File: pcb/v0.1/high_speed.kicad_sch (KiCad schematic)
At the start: 16 parts, among them J4 TYPE_C_Receptacle, J5 TYPE_C_Receptacle, J7 Conn_01x22_Female, U8 AP22653W6-7

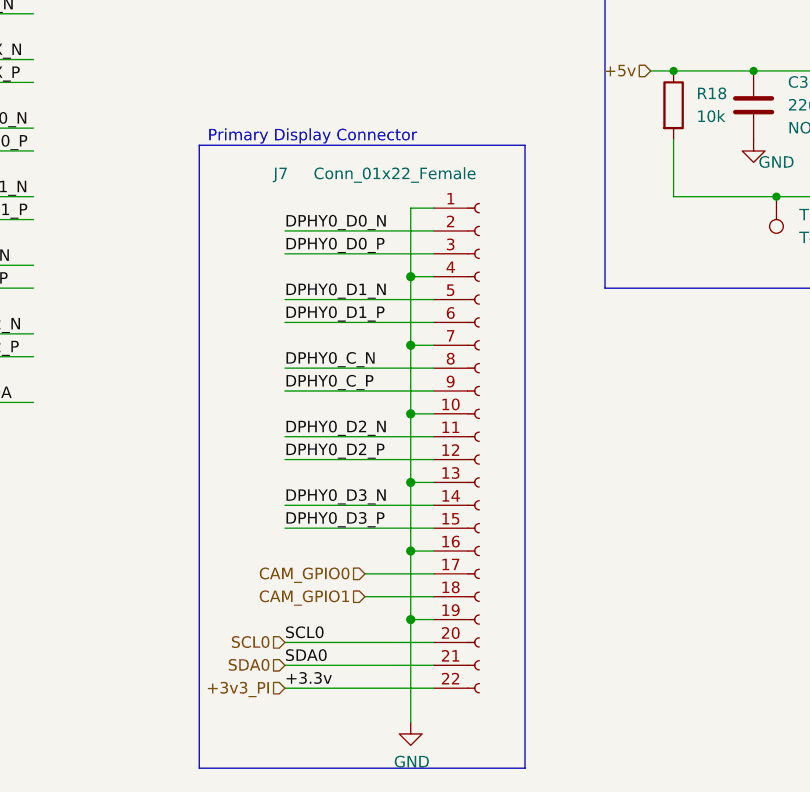
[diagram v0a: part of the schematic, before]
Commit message: Add display connector
The zephyr version is irrelevant now
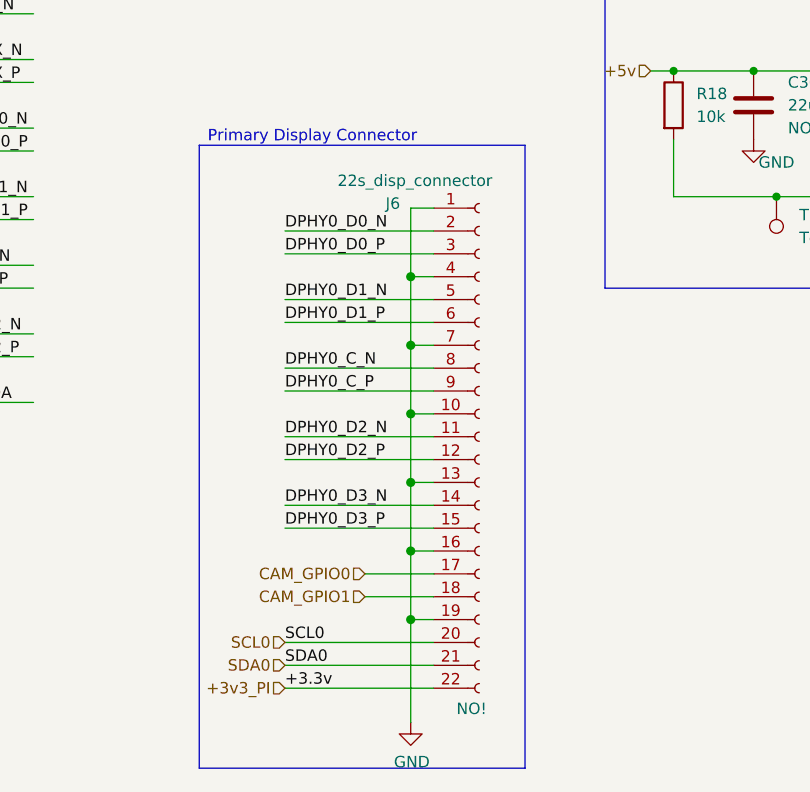
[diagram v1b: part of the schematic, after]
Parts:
- removed J7: Conn_01x22_Female, CM5IO:Hirose_FH12-22S-0.5SH_1x22-1MP_P0.50mm_Horizontal, symbol Connector:Conn_01x22_Socket
- added J6: 22s_disp_connector, symbol TH-1-CC:22s_disp_connector
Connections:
- net +3v3_PI: now also J6.22 (Pin_22)
- net CAM_GPIO0: now also J6.17 (Pin_17)
- net CAM_GPIO1: now also J6.18 (Pin_18)
- net DPHY0_C_N: now also J6.8 (Pin_8)
- net DPHY0_C_P: now also J6.9 (Pin_9)
- net DPHY0_D0_N: now also J6.2 (Pin_2)
- net DPHY0_D0_P: now also J6.3 (Pin_3)
- net DPHY0_D1_N: now also J6.5 (Pin_5)
- net DPHY0_D1_P: now also J6.6 (Pin_6)
- net DPHY0_D2_N: now also J6.11 (Pin_11)
- net DPHY0_D2_P: now also J6.12 (Pin_12)
- net DPHY0_D3_N: now also J6.14 (Pin_14)
- net DPHY0_D3_P: now also J6.15 (Pin_15)
- net GND: now also J6.1 (Pin_1), J6.10 (Pin_10), J6.13 (Pin_13), J6.16 (Pin_16), J6.19 (Pin_19), J6.4 (Pin_4), J6.7 (Pin_7)
- net SCL0: now also J6.20 (Pin_20)
- net SDA0: now also J6.21 (Pin_21)
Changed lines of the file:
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@@
-	)
-	(symbol
-		(lib_id "Connector:Conn_01x22_Socket")
-		(at 167.64 156.21 0)
-		(unit 1)
-		(body_style 1)
-		(exclude_from_sim no)
-		(in_bom yes)
-		(on_board yes)
-		(in_pos_files yes)
-		(dnp no)
-		(property "Reference" "J7"
-			(at 144.78 127 0)
-			(show_name no)
-			(do_not_autoplace no)
-			(effects
-				(font
-					(size 1.27 1.27)
-				)
-				(justify left)
-			)
-		)
-		(property "Value" "Conn_01x22_Female"
-			(at 149.225 127 0)
-			(show_name no)
-			(do_not_autoplace no)
-			(effects
-				(font
-					(size 1.27 1.27)
-				)
-				(justify left)
-			)
-		)
-		(property "Footprint" "CM5IO:Hirose_FH12-22S-0.5SH_1x22-1MP_P0.50mm_Horizontal"
-			(at 167.64 156.21 0)
-			(hide yes)
-			(show_name no)
-			(do_not_autoplace no)
-			(effects
-				(font
-					(size 1.27 1.27)
-				)
-			)
-		)
-		(property "Datasheet" "https://www.hirose.com/product/document?clcode=&productname=&series=FH12&documenttype=Catalog&lang=en&documentid=D31648_en"
-			(at 167.64 156.21 0)
-			(hide yes)
-			(show_name no)
-			(do_not_autoplace no)
-			(effects
-				(font
-					(size 1.27 1.27)
-				)
-			)
-		)
-		(property "Description" ""
-			(at 167.64 156.21 0)
-			(hide yes)
-			(show_name no)
-			(do_not_autoplace no)
-			(effects
-				(font
-					(size 1.27 1.27)
-				)
-			)
-		)
-		(property "Field4" "Mouser"
-			(at 167.64 156.21 0)
-			(hide yes)
-			(show_name no)
-			(do_not_autoplace no)
-			(effects
-				(font
-					(size 1.27 1.27)
-				)
-			)
-		)
-		(property "Field5" "798-FH12-22S-0.5SH55"
-			(at 167.64 156.21 0)
-			(hide yes)
-			(show_name no)
-			(do_not_autoplace no)
-			(effects
-				(font
-					(size 1.27 1.27)
-				)
-			)
-		)
-		(property "Field6" "FH12-22S-0.5SH55"
-			(at 167.64 156.21 0)
-			(hide yes)
-			(show_name no)
-			(do_not_autoplace no)
-			(effects
-				(font
-					(size 1.27 1.27)
-				)
-			)
-		)
-		(property "Field7" "Hirose"
-			(at 167.64 156.21 0)
-			(hide yes)
-			(show_name no)
-			(do_not_autoplace no)
-			(effects
-				(font
-					(size 1.27 1.27)
-				)
-			)
-		)
-		(property "Part Description" "22 Position FFC, FPC Connector Contacts, Bottom 0.020\" (0.50mm) Surface Mount, Right Angle"
-			(at 167.64 156.21 0)
-			(hide yes)
-			(show_name no)
-			(do_not_autoplace no)
-			(effects
-				(font
-					(size 1.27 1.27)
-				)
-			)
-		)
-		(pin "1"
-		)
-		(pin "10"
-		)
-		(pin "11"
-		)
-		(pin "12"
-		)
-		(pin "13"
-		)
-		(pin "14"
-		)
-		(pin "15"
-		)
-		(pin "16"
-		)
-		(pin "17"
-		)
-		(pin "18"
-		)
-		(pin "19"
-		)
-		(pin "2"
-		)
-		(pin "20"
-		)
-		(pin "21"
-		)
-		(pin "22"
-		)
-		(pin "3"
-		)
-		(pin "4"
-		)
-		(pin "5"
-		)
-		(pin "6"
-		)
-		(pin "7"
-		)
-		(pin "8"
-		)
-		(pin "9"
-		)
-		(instances
-			(project "mainboard"
-				(path "/5b8aa782-5c3d-43e7-a869-3bd000015f52/8e613e76-cfa9-4d70-9fba-6dbea9bbdbc9"
-					(reference "J7")
-					(unit 1)
-				)
-			)
-		)
 	)
 	(symbol
@@
 					(unit 1)
 				)
+			)
+		)
+	)
+	(symbol
+		(lib_id "TH-1-CC:22s_disp_connector")
+		(at 167.64 156.21 0)
+		(unit 1)
+		(body_style 1)
+		(exclude_from_sim no)
+		(in_bom yes)
+		(on_board yes)
+		(in_pos_files yes)
+		(dnp no)
+		(property "Reference" "J6"
+			(at 157.226 130.302 0)
+			(show_name no)
+			(do_not_autoplace no)
+			(effects
+				(font
+					(size 1.27 1.27)
+				)
+				(justify left)
+			)
+		)
+		(property "Value" "22s_disp_connector"
+			(at 151.892 127.762 0)
+			(show_name no)
+			(do_not_autoplace no)
+			(effects
+				(font
+					(size 1.27 1.27)
+				)
+				(justify left)
+			)
+		)
+		(property "Footprint" ""
+			(at 167.64 156.21 0)
+			(hide yes)
+			(show_name no)
+			(do_not_autoplace no)
+			(effects
+				(font
+					(size 1.27 1.27)
+				)
+			)
+		)
+		(property "Datasheet" "https://cdn.amphenol-cs.com/media/wysiwyg/files/documentation/datasheet/flex/flexconnectors_050mm_vll.pdf"
+			(at 167.64 156.21 0)
+			(hide yes)
+			(show_name no)
+			(do_not_autoplace no)
+			(effects
+				(font
+					(size 1.27 1.27)
+				)
+			)
+		)
+		(property "Description" "CONN FPC BOTTOM 22POS 0.5MM R/A"
+			(at 167.64 156.21 0)
+			(hide yes)
+			(show_name no)
+			(do_not_autoplace no)
+			(effects
+				(font
+					(size 1.27 1.27)
+				)
+			)
+		)
+		(property "Manufacturer" "Amphenol ICC (FCI)"
+			(at 167.64 156.21 0)
+			(hide yes)
+			(show_name no)
+			(do_not_autoplace no)
+			(effects
+				(font
+					(size 1.27 1.27)
+				)
+			)
+		)
+		(property "Mfr. Part no." "10051922-2210ELF"
+			(at 167.64 156.21 0)
+			(hide yes)
+			(show_name no)
+			(do_not_autoplace no)
+			(effects
+				(font
+					(size 1.27 1.27)
+				)
+			)
+		)
+		(property "Distributor DigiKey" "https://www.digikey.co.uk/en/products/detail/amphenol-cs-fci/10051922-2210ELF/4238683"
+			(at 167.64 156.21 0)
+			(hide yes)
+			(show_name no)
+			(do_not_autoplace no)
+			(effects
+				(font
+					(size 1.27 1.27)
+				)
+			)
+		)
+		(property "Digikey Part no." "609-10051922-2210ELFTR-ND"
+			(at 167.64 156.21 0)
+			(hide yes)
+			(show_name no)
+			(do_not_autoplace no)
+			(effects
+				(font
+					(size 1.27 1.27)
+				)
+			)
+		)
+		(property "Stock" "NO!"
+			(at 165.1 186.436 0)
+			(show_name no)
+			(do_not_autoplace no)
+			(effects
+				(font
+					(size 1.27 1.27)
+				)
+				(justify left)
+			)
+		)
+		(pin "2"
+		)
+		(pin "21"
+		)
+		(pin "20"
+		)
+		(pin "14"
+		)
+		(pin "10"
+		)
+		(pin "18"
+		)
+		(pin "4"
+		)
+		(pin "22"
+		)
+		(pin "11"
+		)
+		(pin "15"
+		)
+		(pin "13"
+		)
+		(pin "19"
+		)
+		(pin "17"
+		)
+		(pin "5"
+		)
+		(pin "8"
+		)
+		(pin "6"
+		)
+		(pin "3"
+		)
+		(pin "1"
+		)
+		(pin "12"
+		)
+		(pin "9"
+		)
+		(pin "7"
+		)
+		(pin "16"
+		)
+		(instances
+			(project "mainboard"
+				(path "/5b8aa782-5c3d-43e7-a869-3bd000015f52/8e613e76-cfa9-4d70-9fba-6dbea9bbdbc9"
+					(reference "J6")
+					(unit 1)
+				)

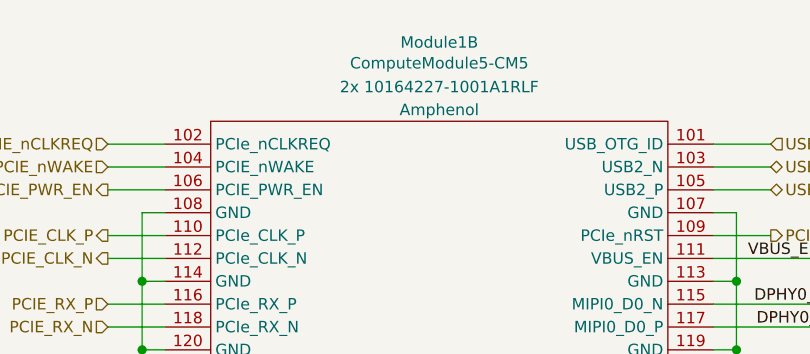
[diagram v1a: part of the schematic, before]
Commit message: Add connector for CM5
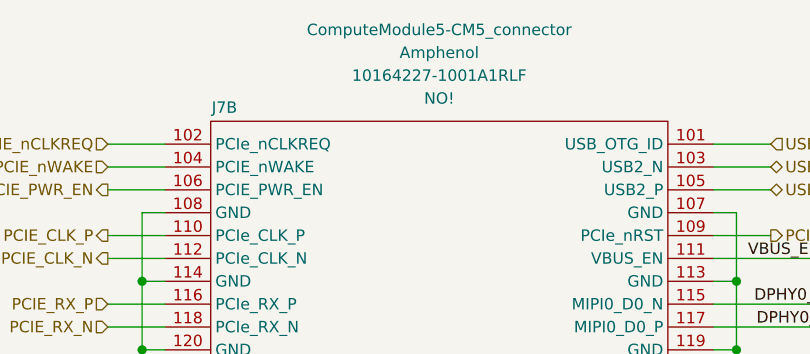
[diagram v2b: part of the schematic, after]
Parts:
- removed Module1: ComputeModule5-CM5, CM5IO:Raspberry-Pi-5-Compute-Module, symbol CM5IO:ComputeModule5-CM5
- added J7: ComputeModule5-CM5_connector, symbol TH-1-CC:ComputeModule5-CM5_connectors
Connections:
- net DPHY0_C_N: now also J7.127 (MIPI0_C_N)
- net DPHY0_C_P: now also J7.129 (MIPI0_C_P)
- net DPHY0_D0_N: now also J7.115 (MIPI0_D0_N)
- net DPHY0_D0_P: now also J7.117 (MIPI0_D0_P)
- net DPHY0_D1_N: now also J7.121 (MIPI0_D1_N)
- net DPHY0_D1_P: now also J7.123 (MIPI0_D1_P)
- net DPHY0_D2_N: now also J7.133 (MIPI0_D2_N)
- net DPHY0_D2_P: now also J7.135 (MIPI0_D2_P)
- net DPHY0_D3_N: now also J7.139 (MIPI0_D3_N)
- net DPHY0_D3_P: now also J7.141 (MIPI0_D3_P)
- net DPHY1_C_N: now also J7.187 (MIPI1_C_N)
- net DPHY1_C_P: now also J7.189 (MIPI1_C_P)
- net DPHY1_D0_N: now also J7.175 (MIPI1_D0_N)
- net DPHY1_D0_P: now also J7.177 (MIPI1_D0_P)
- net DPHY1_D1_N: now also J7.181 (MIPI1_D1_N)
- net DPHY1_D1_P: now also J7.183 (MIPI1_D1_P)
- net DPHY1_D2_N: now also J7.193 (MIPI1_D2_N)
- net DPHY1_D2_P: now also J7.195 (MIPI1_D2_P)
- net DPHY1_D3_N: now also J7.194 (MIPI1_D3_N)
- net DPHY1_D3_P: now also J7.196 (MIPI1_D3_P)
- net GND: now also J7.107 (GND), J7.108 (GND), J7.113 (GND), J7.114 (GND), J7.119 (GND), J7.120 (GND), J7.125 (GND), J7.126 (GND), J7.131 (GND), J7.132 (GND), J7.137 (GND), J7.138 (GND), J7.144 (GND), J7.150 (GND), J7.155 (GND), J7.156 (GND), J7.161 (GND), J7.162 (GND), J7.167 (GND), J7.168 (GND), J7.173 (GND), J7.174 (GND), J7.179 (GND), J7.180 (GND), J7.185 (GND), J7.186 (GND), J7.191 (GND), J7.192 (GND), J7.197 (GND), J7.198 (GND)
- net HDMI0_CEC: now also J7.151 (HDMI0_CEC)
- net HDMI0_CK_N: now also J7.190 (HDMI0_CLK_N)
- net HDMI0_CK_P: now also J7.188 (HDMI0_CLK_P)
- net HDMI0_D0_N: now also J7.184 (HDMI0_TX0_N)
- net HDMI0_D0_P: now also J7.182 (HDMI0_TX0_P)
- net HDMI0_D1_N: now also J7.178 (HDMI0_TX1_N)
- net HDMI0_D1_P: now also J7.176 (HDMI0_TX1_P)
- net HDMI0_D2_N: now also J7.172 (HDMI0_TX2_N)
- net HDMI0_D2_P: now also J7.170 (HDMI0_TX2_P)
- net HDMI0_HOTPLUG: now also J7.153 (HDMI0_HOTPLUG)
- net HDMI0_SCL: now also J7.200 (HDMI0_SCL)
- net HDMI0_SDA: now also J7.199 (HDMI0_SDA)
- net HDMI1_CEC: now also J7.149 (HDMI1_CEC)
- net HDMI1_CK_N: now also J7.166 (HDMI1_CLK_N)
- net HDMI1_CK_P: now also J7.164 (HDMI1_CLK_P)
- net HDMI1_D0_N: now also J7.160 (HDMI1_TX0_N)
- net HDMI1_D0_P: now also J7.158 (HDMI1_TX0_P)
- net HDMI1_D1_N: now also J7.154 (HDMI1_TX1_N)
- net HDMI1_D1_P: now also J7.152 (HDMI1_TX1_P)
- net HDMI1_D2_N: now also J7.148 (HDMI1_TX2_N)
- net HDMI1_D2_P: now also J7.146 (HDMI1_TX2_P)
- net HDMI1_HOTPLUG: now also J7.143 (HDMI1_HOTPLUG)
- net HDMI1_SCL: now also J7.147 (HDMI1_SCL)
- net HDMI1_SDA: now also J7.145 (HDMI1_SDA)
- net PCIE_CLK_N: now also J7.112 (PCIe_CLK_N)
- net PCIE_CLK_P: now also J7.110 (PCIe_CLK_P)
- net PCIE_PWR_EN: now also J7.106 (PCIE_PWR_EN)
- net PCIE_RX_N: now also J7.118 (PCIe_RX_N)
- net PCIE_RX_P: now also J7.116 (PCIe_RX_P)
- net PCIE_TX_N: now also J7.124 (PCIe_TX_N)
- net PCIE_TX_P: now also J7.122 (PCIe_TX_P)
- net PCIE_nCLKREQ: now also J7.102 (PCIe_nCLKREQ)
- net PCIE_nRST: now also J7.109 (PCIe_nRST)
- net PCIE_nWAKE: now also J7.104 (PCIE_nWAKE)
- net USB2_N: now also J7.103 (USB2_N)
- net USB2_P: now also J7.105 (USB2_P)
- net USB3-0-D_N: now also J7.136 (USB3-0-D_N)
- net USB3-0-D_P: now also J7.134 (USB3-0-D_P)
- net USB3-0-RX_N: now also J7.128 (USB3-0-RX_N)
- net USB3-0-RX_P: now also J7.130 (USB3-0-RX_P)
- net USB3-0-TX_N: now also J7.140 (USB3-0-TX_N)
- net USB3-0-TX_P: now also J7.142 (USB3-0-TX_P)
- net USB3-1-D_N: now also J7.165 (USB3-1-D_N)
- net USB3-1-D_P: now also J7.163 (USB3-1-D_P)
- net USB3-1-RX_N: now also J7.157 (USB3-1-RX_N)
- net USB3-1-RX_P: now also J7.159 (USB3-1-RX_P)
- net USB3-1-TX_N: now also J7.169 (USB3-1-TX_N)
- net USB3-1-TX_P: now also J7.171 (USB3-1-TX_P)
- net USBOTG_ID: now also J7.101 (USB_OTG_ID)
- net VBUS_EN: now also J7.111 (VBUS_EN)

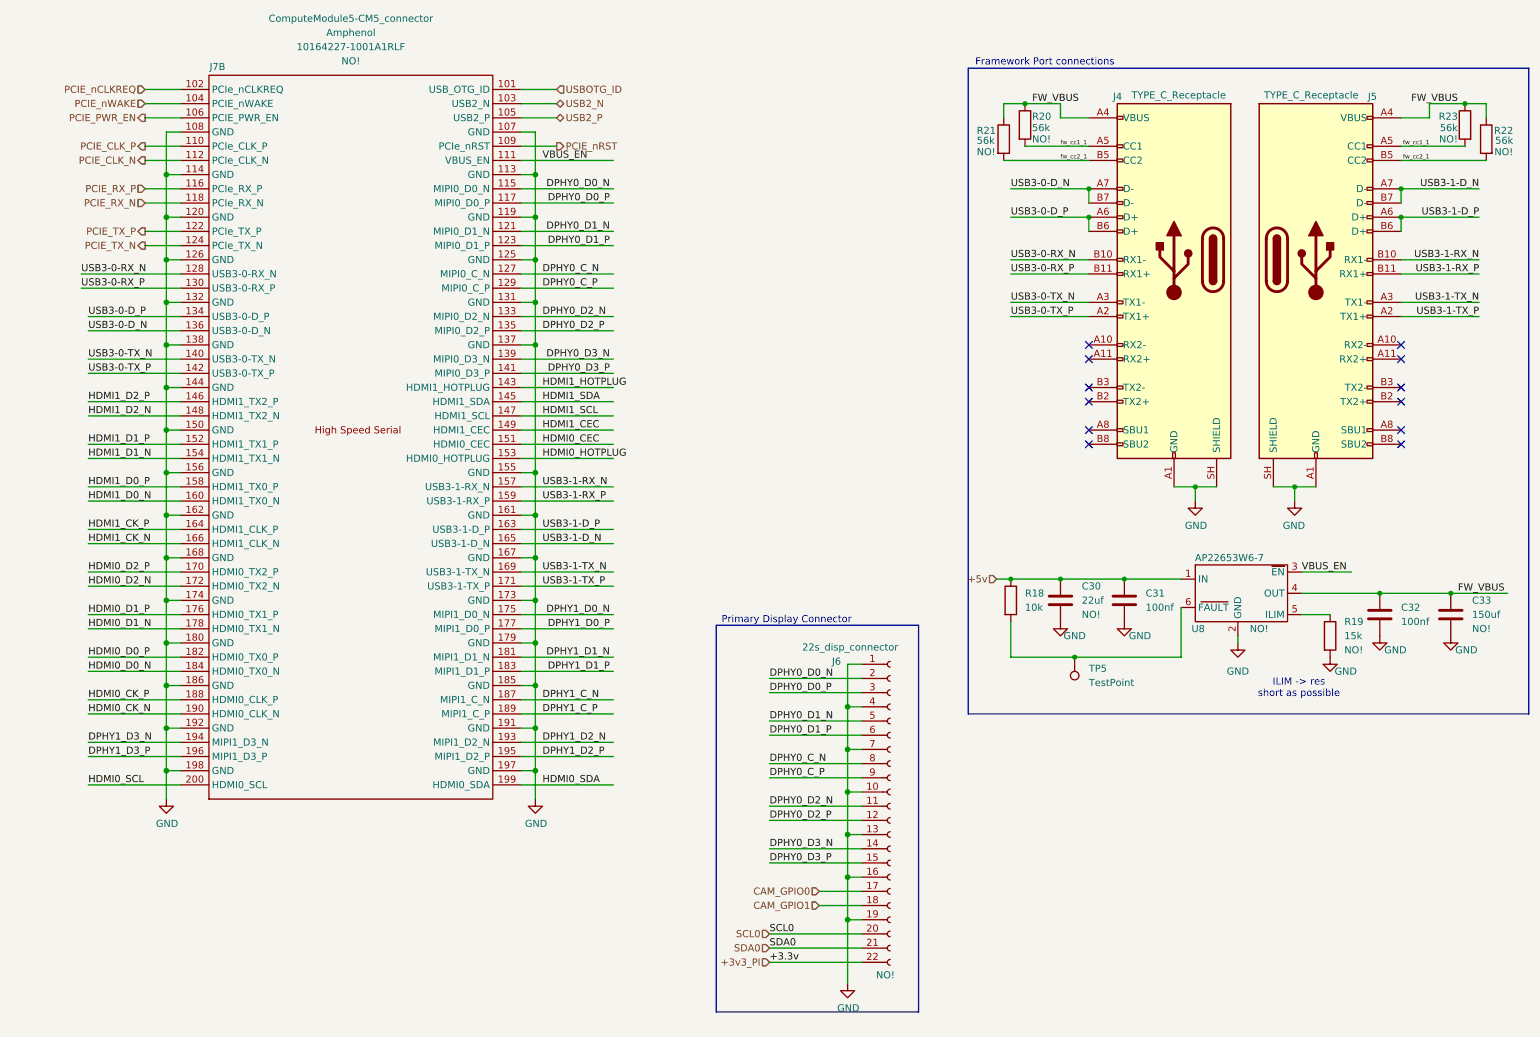
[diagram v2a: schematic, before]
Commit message: High speed and Super speed ESD arrays
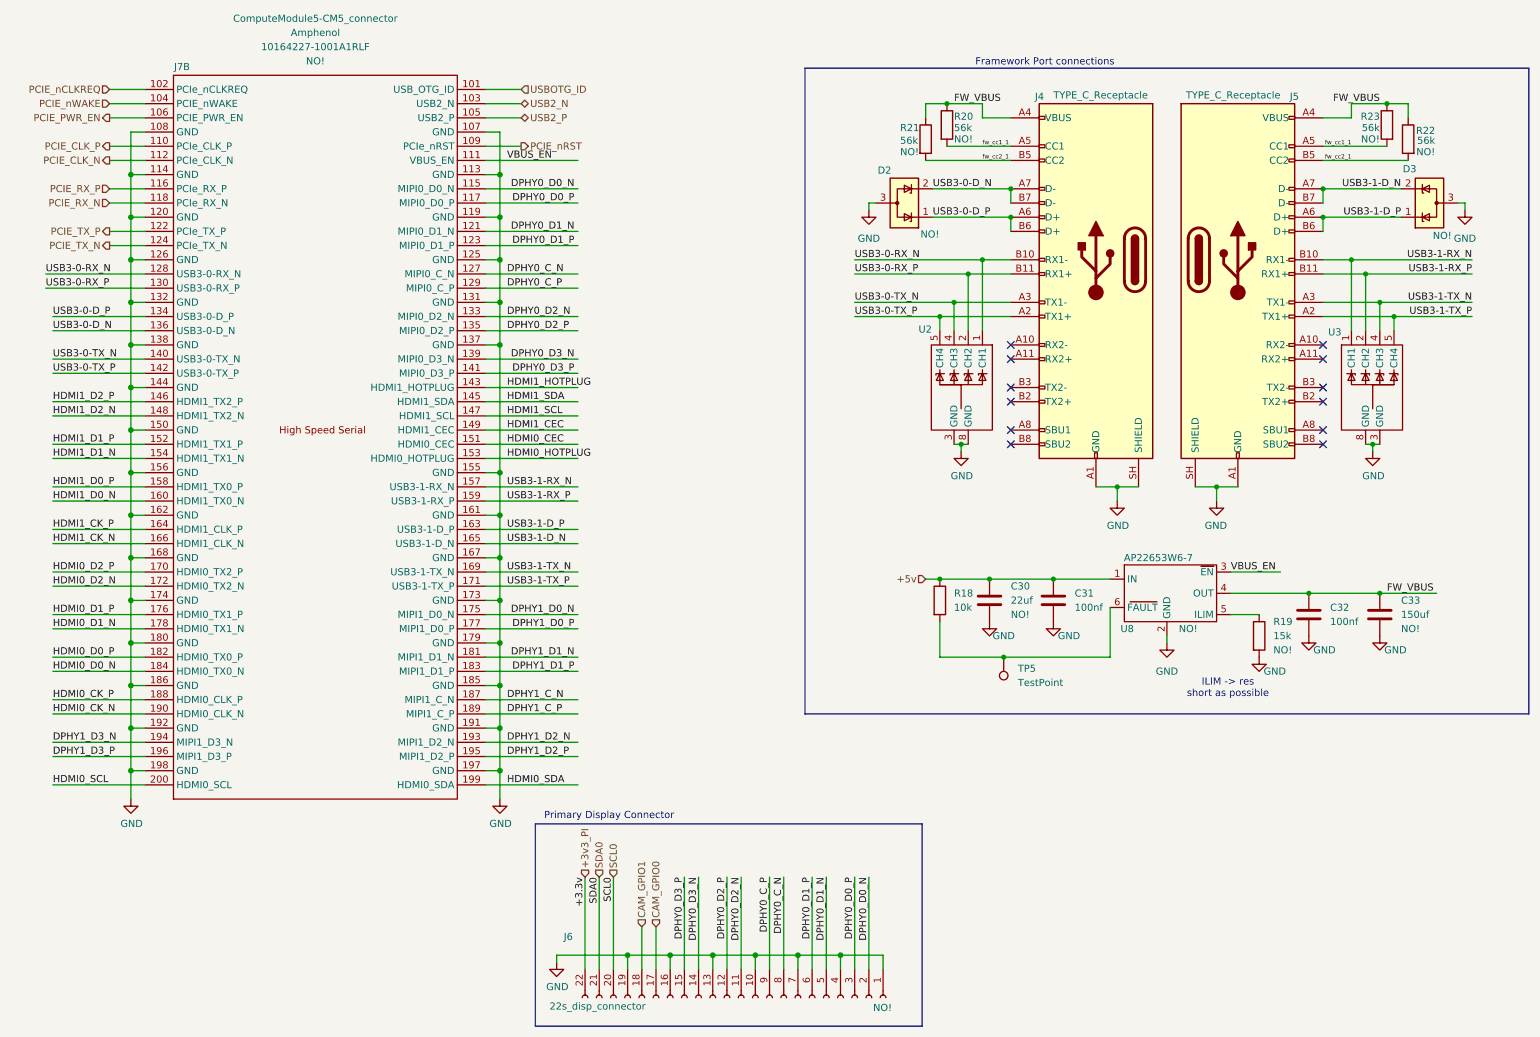
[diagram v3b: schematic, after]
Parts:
- added D2, D3: TECH REPUBLIC ESD5302F, Package_TO_SOT_SMD:SOT-23, symbol TH-1-CC:High_speed_TVS_array
- added U2, U3: Nexperia PUSB3FR4Z, symbol TH-1-CC:Super_Speed_TVS_array
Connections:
- net GND: now also D2.3 (GND), D3.3 (GND), U2.3 (GND), U2.8 (GND), U3.3 (GND), U3.8 (GND)
- net USB3-0-D_N: now also D2.2 (IO2)
- net USB3-0-D_P: now also D2.1 (IO1)
- net USB3-0-RX_N: now also U2.1 (CH1)
- net USB3-0-RX_P: now also U2.2 (CH2)
- net USB3-0-TX_N: now also U2.4 (CH3)
- net USB3-0-TX_P: now also U2.5 (CH4)
- net USB3-1-D_N: now also D3.2 (IO2)
- net USB3-1-D_P: now also D3.1 (IO1)
- net USB3-1-RX_N: now also U3.1 (CH1)
- net USB3-1-RX_P: now also U3.2 (CH2)
- net USB3-1-TX_N: now also U3.4 (CH3)
- net USB3-1-TX_P: now also U3.5 (CH4)
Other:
- moved on the sheet: C30, C31, C32, C33, J4, J5, J6, J7B, R18, R19, R20, R21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
